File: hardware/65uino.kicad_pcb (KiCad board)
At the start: 2 copper layers, 74.9 x 53.3 mm, 55 parts, among them J1 Barrel_Jack_MountingPin, J2 USB_B_Micro, J3 OLED, SW1 RST, SW2 BTN, U1 R6507, U2 NC/74HC04, U3 6532, U4 w27C512, U5 MIC5504-3.3YM5, U6 LM1117-5.0, U7 SN74LVC1G14DBVR, X1 1MHz, Y1 NC/1Mhz

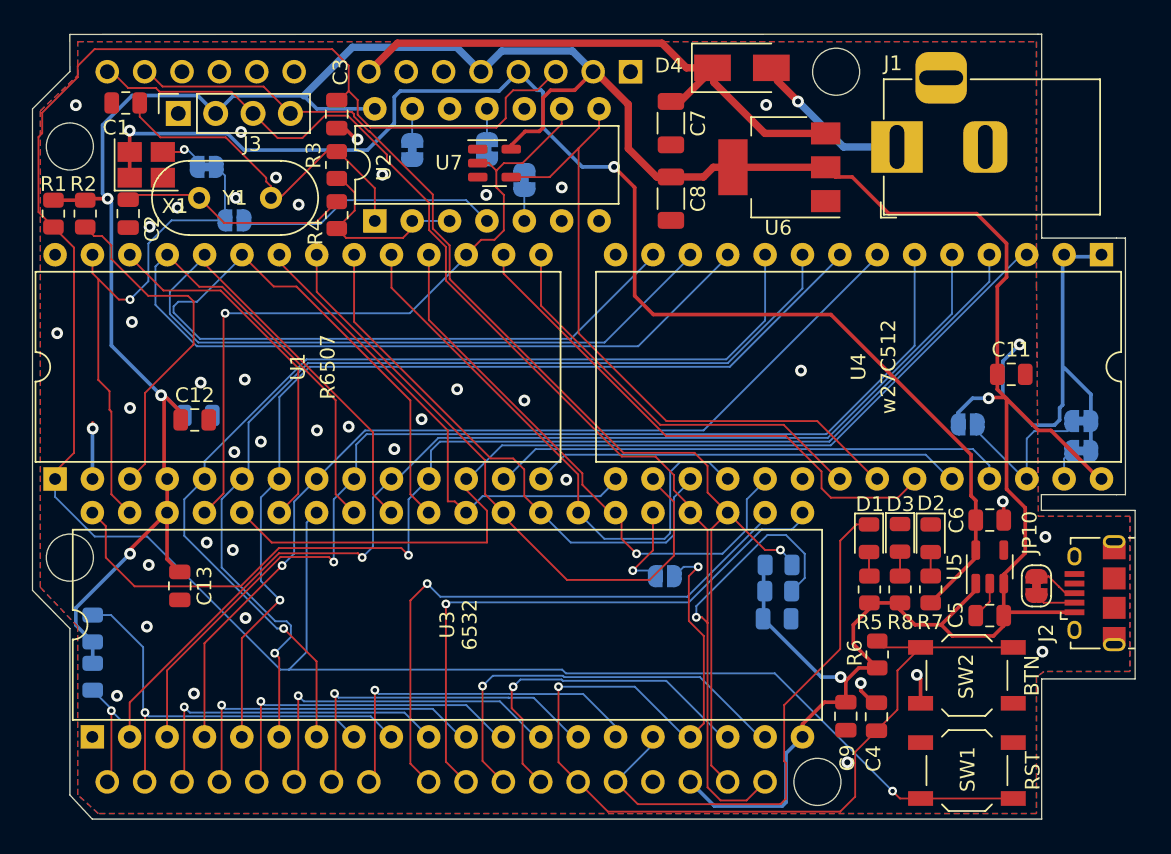
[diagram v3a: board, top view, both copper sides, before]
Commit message: Revision 1 - UART & Clock Divider
UART, Clock Divider, extra address decoding and bus headers added - a full-fledged 6502 computer with an Uno footprint!
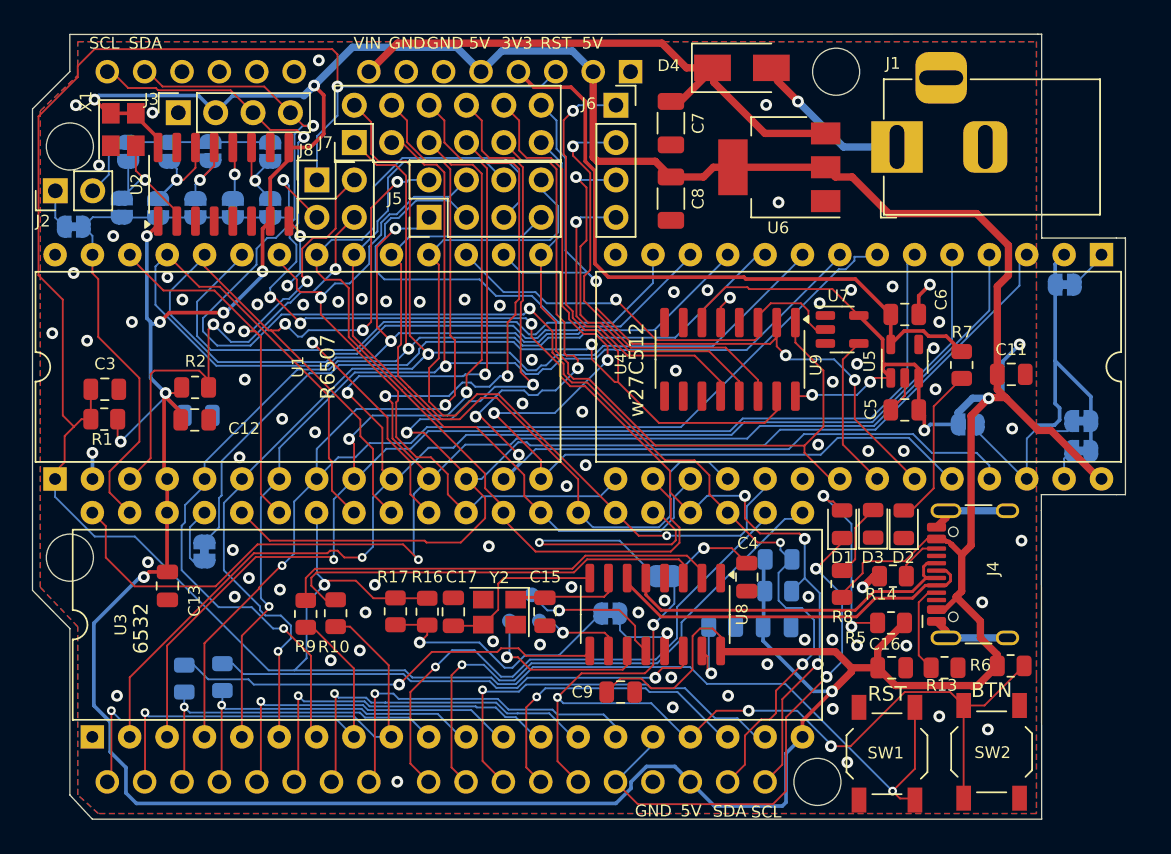
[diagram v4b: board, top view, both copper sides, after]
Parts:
- removed C1, C2: NC/30pF, Capacitor_SMD:C_0805_2012Metric
- removed Y1: NC/1Mhz, Crystal:Crystal_HC49-U_Vertical
- added C15: 22p, Capacitor_SMD:C_0805_2012Metric, F.Cu at (136.8, 87.8)
- added C16: 1uF, Capacitor_SMD:C_0805_2012Metric, F.Cu at (160.3, 91.6)
- added C17: 22p, Capacitor_SMD:C_0805_2012Metric, F.Cu at (130.6, 87.8)
- added J4: USB2.0_16P, Connector_USB:USB_C_Receptacle_HCTL_HC-TYPE-C-16P-01A, F.Cu at (167.1, 85.2)
- added J5: Databus, Connector_PinHeader_2.54mm:PinHeader_2x04_P2.54mm_Vertical, F.Cu at (128.9, 61.0)
- added J6: Chip select, Connector_PinSocket_2.54mm:PinSocket_1x04_P2.54mm_Vertical, F.Cu at (141.6, 53.3)
- added J7: Addressbus, Connector_PinHeader_2.54mm:PinHeader_2x06_P2.54mm_Vertical, F.Cu at (123.8, 55.9)
- added J8: Signals, Connector_PinHeader_2.54mm:PinHeader_2x02_P2.54mm_Vertical, F.Cu at (121.3, 58.4)
- added JP11: SolderJumper_2_Bridged, Jumper:SolderJumper-2_P1.3mm_Open_RoundedPad1.0x1.5mm, B.Cu at (108.5, 56.5)
- added JP12: SolderJumper_2_Bridged, Jumper:SolderJumper-2_P1.3mm_Open_RoundedPad1.0x1.5mm, B.Cu at (111.3, 56.5)
- added JP13: SolderJumper_2_Bridged, Jumper:SolderJumper-2_P1.3mm_Open_RoundedPad1.0x1.5mm, B.Cu at (114.0, 56.5)
- added JP14: SolderJumper_2_Bridged, Jumper:SolderJumper-2_P1.3mm_Open_RoundedPad1.0x1.5mm, B.Cu at (118.1, 56.5)
- added JP15: SolderJumper_2_Bridged, Jumper:SolderJumper-2_P1.3mm_Bridged_RoundedPad1.0x1.5mm, B.Cu at (104.8, 61.6)
- added JP16: SolderJumper_2_Bridged, Jumper:SolderJumper-2_P1.3mm_Bridged_RoundedPad1.0x1.5mm, B.Cu at (141.2, 87.9)
- added JP17: SolderJumper_2_Bridged, Jumper:SolderJumper-2_P1.3mm_Bridged_RoundedPad1.0x1.5mm, B.Cu at (113.6, 83.7)
- added R13: 5k1, Resistor_SMD:R_0805_2012Metric, F.Cu at (163.9, 91.6)
- added R14: 5k1, Resistor_SMD:R_0805_2012Metric, F.Cu at (160.4, 85.3)
- added R15: NC, Resistor_SMD:R_0805_2012Metric, B.Cu at (148.8, 88.8)
- added R16: 1k, Resistor_SMD:R_0805_2012Metric, F.Cu at (128.8, 87.8)
- added R17: 1k, Resistor_SMD:R_0805_2012Metric, F.Cu at (126.6, 87.7)
- added TP1: ~{RI}, TestPoint:TestPoint_Pad_D1.0mm, B.Cu at (134.4, 88.4)
- added TP2: ~{DCD}, TestPoint:TestPoint_Pad_D1.0mm, B.Cu at (135.9, 86.6)
- added TP3: ~{DSR}, TestPoint:TestPoint_Pad_D1.0mm, B.Cu at (136.4, 88.4)
- added U8: CH340G, Package_SO:SOIC-16_3.9x9.9mm_P1.27mm, F.Cu at (144.3, 87.9)
- added U9: 74HC138, Package_SO:SOP-16_3.9x9.9mm_P1.27mm, F.Cu at (149.4, 70.6)
- added Y2: 12MHz, Crystal:Crystal_SMD_3225-4Pin_3.2x2.5mm, F.Cu at (133.7, 87.8)
- D3: value WHITE LED -> RED LED
- J1: value Barrel_Jack_MountingPin -> Barrel
- J2: value USB_B_Micro -> GPCO; footprint Connector_USB:USB_Micro-B_Amphenol_10118194_Horizontal -> Connector_PinHeader_2.54mm:PinHeader_1x02_P2.54mm_Vertical
- JP10: moved to B.Cu
- JP3, JP4, JP5: footprint Jumper:SolderJumper-2_P1.3mm_Bridged_RoundedPad1.0x1.5mm -> Jumper:SolderJumper-2_P1.3mm_Open_RoundedPad1.0x1.5mm
- R10, R9: value NC -> 1k; moved to F.Cu
- R3: value NC/1M -> NC; moved to B.Cu
- R4: value NC/470 -> NC; moved to B.Cu
- U2: value NC/74HC04 -> 74HC161; footprint Package_DIP:DIP-14_W7.62mm -> Package_SO:SOP-16_3.9x9.9mm_P1.27mm
- U6: value LM1117-5.0 -> AMS1117-5.0
- X1: value 1MHz -> 8MHz; footprint Oscillator:Oscillator_SMD_SeikoEpson_SG210-4Pin_2.5x2.0mm_HandSoldering -> Crystal:Crystal_SMD_3225-4Pin_3.2x2.5mm
- moved J2 75.8 mm to (103.5, 59.2)
- moved R3 36.4 mm to (112.3, 92.3)
- moved R4 32.3 mm to (114.9, 92.2)
- moved U7 26.2 mm to (157.0, 68.6)
- moved C3 24.5 mm to (106.9, 72.6), turned to 180 degrees
- moved JP5 22.7 mm to (110.5, 60.3), turned to -90 degrees
- moved JP10 20.6 mm to (172.1, 65.5), turned to 0 degrees
- moved JP3 17.4 mm to (118.1, 60.3)
- moved R10 16.5 mm to (122.6, 87.9), turned to 90 degrees
- moved R7 15.4 mm to (165.1, 71.0), turned to 90 degrees
- moved C9 15.4 mm to (141.9, 93.2), turned to 0 degrees
- moved JP4 15.2 mm to (113.0, 60.3), turned to -90 degrees
- moved C6 15.1 mm to (161.2, 67.6)
- moved C5 15.1 mm to (161.2, 74.0)
- moved U5 15.1 mm to (161.2, 70.7)
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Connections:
- net Net-(R2-Pad2) renamed /RDY
- net Net-(U1-Pad26) renamed /~{RW}
- J2 pad 1: +5V -> Net-(J2-Pin_1)
- J2 pad 2: Net-(J2-Pad2) -> Net-(J2-Pin_2)
- JP10 pad 1: Net-(J2-Pad2) -> GND
- JP10 pad 2: Net-(J2-Pad3) -> Net-(JP10-B)
- JP3 pad 1: GND -> 500KHz
- JP3 pad 2: Net-(JP3-Pad2) -> /PHI0
- JP4 pad 1: GND -> 2Mhz
- JP4 pad 2: Net-(JP4-Pad2) -> /PHI0
- JP5 pad 1: GND -> 4Mhz
- JP5 pad 2: Net-(JP5-Pad2) -> /PHI0
- JP6 pad 1: Net-(JP6-Pad1) -> 8Mhz
- JP7 pad 1: Net-(JP7-Pad1) -> 1Mhz
- R10 pad 2: +5V -> /RXD
- R3 pad 1: Net-(R3-Pad1) -> /PA2/D2
- R3 pad 2: Net-(C1-Pad1) -> /~{CTS}
- R4 pad 1: Net-(R3-Pad1) -> /PA3/D3
- R4 pad 2: Net-(C2-Pad1) -> /~{RTS}
- R9 pad 2: +5V -> /TXD
- U2 pad 1: Net-(C1-Pad1) -> +5V
- U2 pad 11: Net-(JP5-Pad2) -> 500KHz
- U2 pad 12: unconnected-(U2-Pad12) -> 1Mhz
- U2 pad 13: Net-(JP4-Pad2) -> 2Mhz
- U2 pad 14: +5V -> 4Mhz
- U2 pad 2: Net-(R3-Pad1) -> 8Mhz
- U2 pad 3: Net-(R3-Pad1) -> unconnected-(U2-D0-Pad3)
- U2 pad 4: Net-(JP6-Pad1) -> unconnected-(U2-D1-Pad4)
- U2 pad 5: Net-(JP3-Pad2) -> unconnected-(U2-D2-Pad5)
- U2 pad 7: GND -> +5V
- U2 pad 8: Net-(U2-Pad8) -> GND
- U2 pad 9: A12 -> +5V
- U3 pad 37: A12 -> Net-(JP17-A)
- U4 pad 1: GND -> Net-(JP10-B)
- U4 pad 22: Net-(U2-Pad8) -> Net-(U4-~{OE})
- U7 pad 4: Net-(U2-Pad8) -> Net-(U4-~{OE})
- X1 pad 1: +3V3 -> +5V
- X1 pad 3: Net-(JP7-Pad1) -> 8Mhz
- X1 pad 4: +3V3 -> +5V
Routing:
- net +5V: track 237.0 -> 355.5 mm, vias 5 -> 14
- net /6532_CS: track 0.00 -> 75.5 mm, vias 0 -> 2
- net Net-(U2-Pad8): track 45.7 -> 0.00 mm
- net +3V3: track 91.2 -> 46.0 mm, vias 2 -> 0
- net A5: track 74.8 -> 114.9 mm, vias 1 -> 3
- net A9: track 29.4 -> 67.0 mm, vias 0 -> 2
- net A7: track 66.1 -> 103.4 mm, vias 0 -> 2
- net A6: track 78.2 -> 113.9 mm, vias 1 -> 3
- net A3: track 64.8 -> 100.1 mm, vias 1 -> 2
- net A8: track 35.2 -> 69.5 mm, vias 0 -> 3
- net /~{RTS}: track 0.00 -> 33.7 mm, vias 0 -> 1
- net A4: track 74.5 -> 107.1 mm, vias 1 -> 3
- net /TXD: track 0.00 -> 29.5 mm
- net /RXD: track 0.00 -> 29.5 mm
- net /~{CTS}: track 0.00 -> 29.4 mm, vias 0 -> 1
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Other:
- board size 74.9 x 53.3 mm -> 74.3 x 53.3 mm
- board text added: "$0000"
- board text added: "$0400"
- board text added: "$0800"
- board text added: "$0C00"
- board text added: ".5M"
- board text added: "18V Max!"
- board text added: "1M"
- board text added: "2M"
- board text added: "4M"
- board text added: "6532 IRQ"
- board text added: "6532 ~{CS}"
- board text added: "65uino rev 1 ABNielsen.com/65uino"
- board text added: "8MHz"
- board text added: "A0"
- board text added: "A1"
- board text added: "A10"
- board text added: "A11"
- board text added: "D0"
- board text added: "D1"
- board text added: "D6"
- board text added: "D7"
- board text added: "PB6"
- board text added: "RDY"
- board text added: "~{DTR}"
- board text removed: "65uino rev 0 ABNielsen.com/65uino"

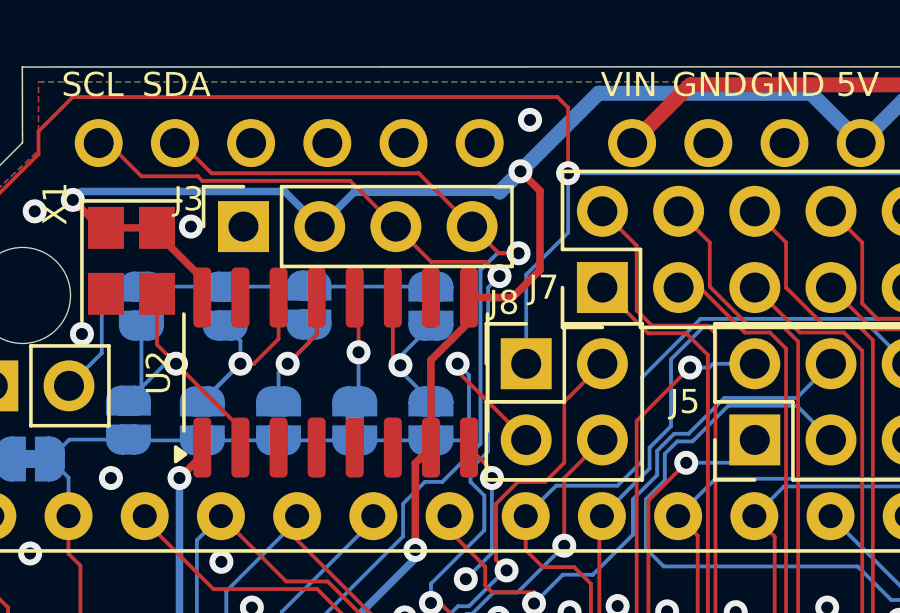
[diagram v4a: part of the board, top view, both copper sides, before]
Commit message: Rev1 Gerber Fix
Connect U2 pin 9 and 10 for stable oscillator performance without solder blob
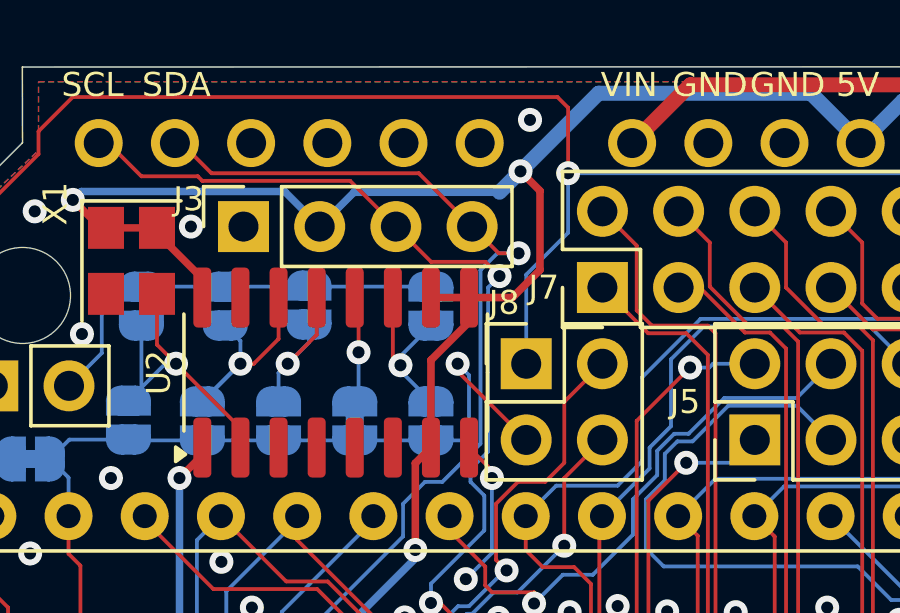
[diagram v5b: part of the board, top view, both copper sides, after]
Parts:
- R7: value 15k -> 22k
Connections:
- U2 pad 10: unconnected-(U2-CET-Pad10) -> +5V
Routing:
- net +5V: track 355.5 -> 356.7 mm

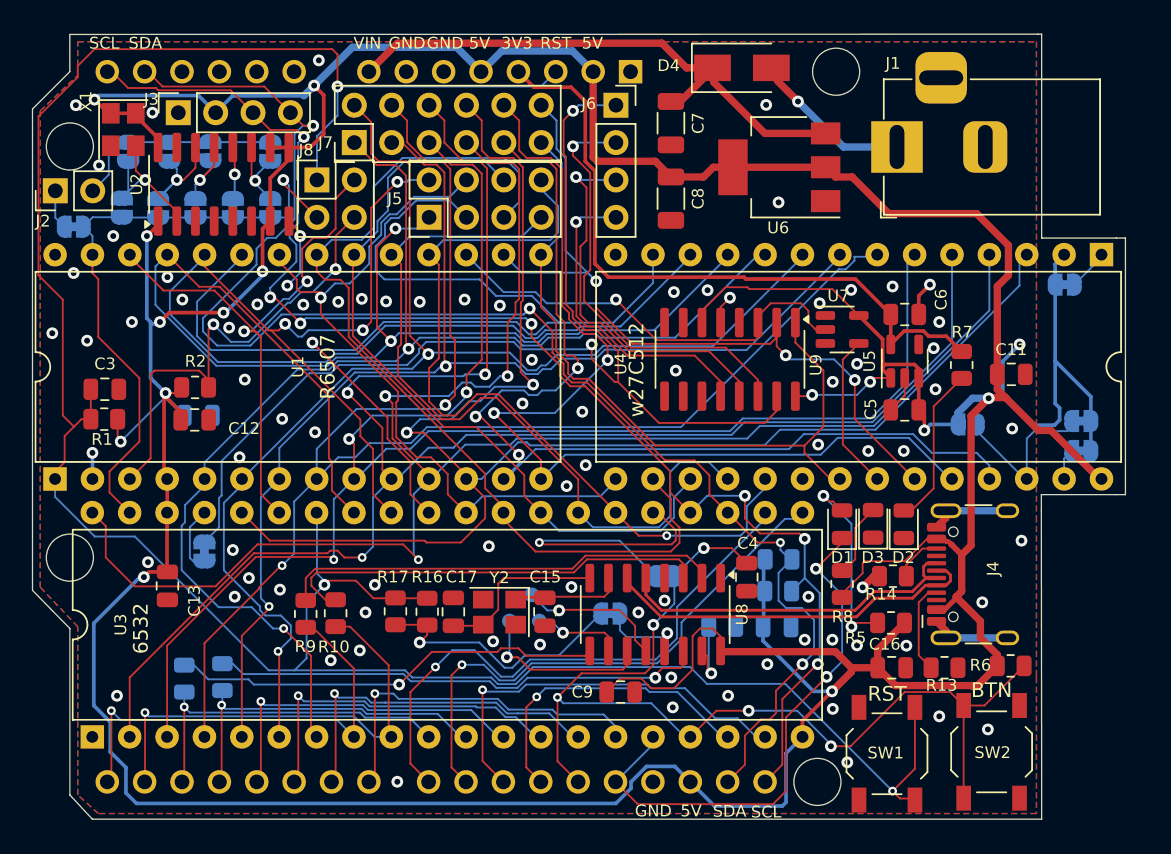
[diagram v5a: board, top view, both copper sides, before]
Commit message: Rev 1.1
Rev 1.1 - working i2c scanner, default baud rate 4800, SOT23 EEPROM added
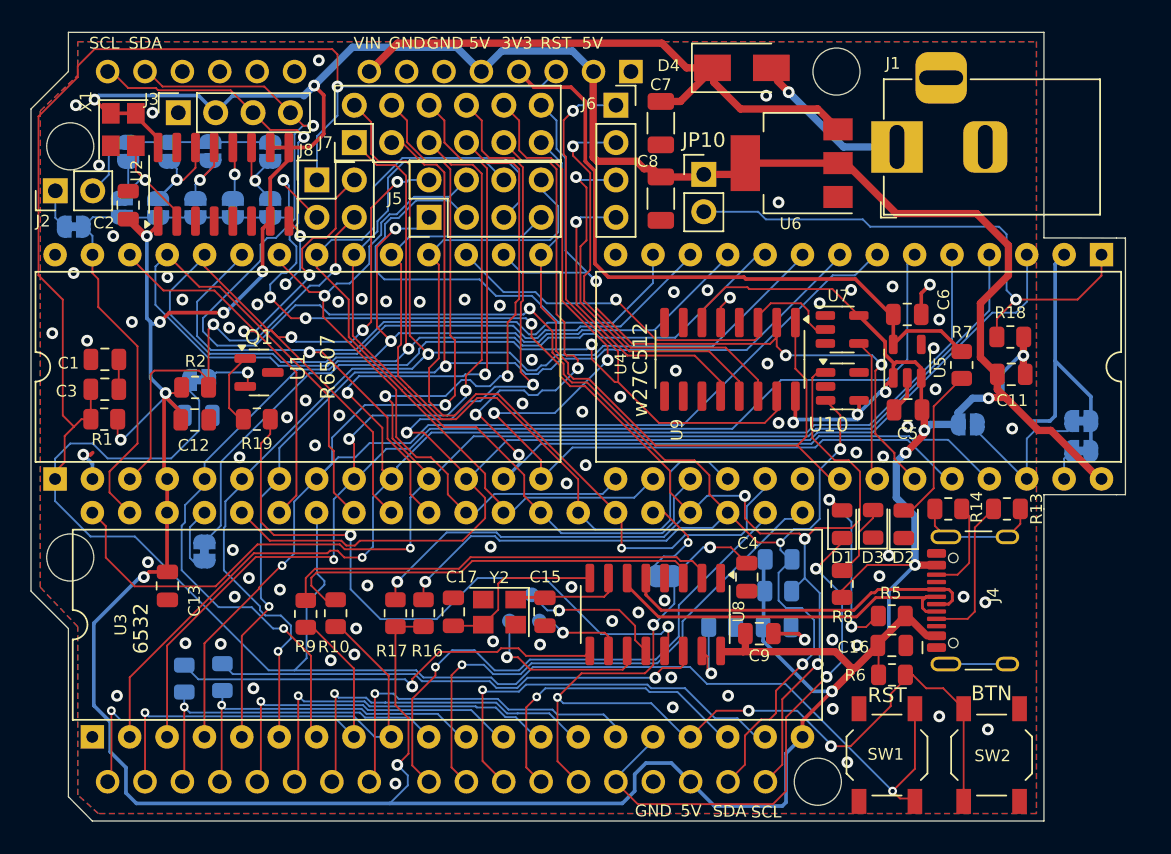
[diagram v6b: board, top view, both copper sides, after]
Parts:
- added C1: 100nF, Capacitor_SMD:C_0805_2012Metric, F.Cu at (106.9, 70.6)
- added C2: 100nF, Capacitor_SMD:C_0805_2012Metric, F.Cu at (108.5, 60.1)
- added Q1: MMBT3906, Package_TO_SOT_SMD:SOT-23, F.Cu at (117.3, 71.5)
- added R18: 22k, Resistor_SMD:R_0805_2012Metric, F.Cu at (168.4, 69.1)
- added R19: 1k, Resistor_SMD:R_0805_2012Metric, F.Cu at (117.2, 74.7)
- added U10: 24C64S, Package_TO_SOT_SMD:SOT-23-5, F.Cu at (157.0, 72.5)
- JP10: value SolderJumper_2_Bridged -> Jumper; footprint Jumper:SolderJumper-2_P1.3mm_Bridged_RoundedPad1.0x1.5mm -> Connector_PinHeader_2.54mm:PinHeader_1x02_P2.54mm_Vertical; moved to F.Cu
- R16, R17: value 1k -> 5k1
- moved JP16 32.1 mm to (113.3, 72.0)
- moved JP10 25.6 mm to (147.6, 58.0)
- moved R13 11.6 mm to (168.2, 80.8)
- moved C9 10.2 mm to (151.3, 89.2)
- moved R6 8.09 mm to (160.4, 92.0)
- moved R14 5.92 mm to (164.2, 80.8)
- moved J4 1.78 mm to (167.1, 87.0)
- moved C16 1.52 mm to (160.3, 90.0)
- moved U6 0.88 mm to (153.5, 57.3)
- moved C7 0.69 mm to (144.7, 54.6)
- moved C8 0.69 mm to (144.7, 59.7)
- moved R5 0.47 mm to (160.3, 88.0)
- moved R16 0.27 mm to (128.5, 87.9)
- moved C5 0.22 mm to (161.4, 74.0)
- moved SW2 0.22 mm to (167.1, 97.5)
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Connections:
- C3 pad 1: GND -> Net-(C1-Pad2)
- JP10 pad 1: GND -> +5V
- JP16 pad 1: /~{DTR} -> Net-(JP16-A)
- JP16 pad 2: Net-(JP16-B) -> /RST
- R16 pad 1: /RST -> /SDA
- R16 pad 2: Net-(JP16-B) -> +5V
- R17 pad 1: /RST -> /SCL
- R17 pad 2: Net-(JP16-B) -> +5V
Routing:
- net /SCL: track 93.9 -> 133.4 mm, vias 7 -> 8
- net /~{DTR}: track 5.95 -> 44.5 mm, vias 1 -> 2
- net /SDA: track 101.4 -> 138.3 mm, vias 4 -> 6
- net Net-(JP10-B): track 2.62 -> 36.9 mm, vias 0 -> 1
- net Net-(JP16-B): track 18.1 -> 0.00 mm, vias 1 -> 0
- net Net-(JP9-B): track 20.2 -> 6.53 mm
- net /RST: track 171.3 -> 180.3 mm, vias 3 -> 2
- net D4: track 63.0 -> 54.9 mm
- net Net-(Q1-B): track 0.00 -> 4.89 mm
- net Net-(J4-CC1): track 5.72 -> 10.3 mm
- net GND: track 53.6 -> 57.8 mm, vias 85 -> 88
- net /PB6/D12: track 70.1 -> 66.3 mm
- net Net-(JP16-A): track 0.00 -> 3.64 mm, vias 0 -> 1
- net Net-(J4-CC2): track 3.28 -> 6.44 mm
- net /VIN: track 38.2 -> 40.3 mm
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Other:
- board size 74.3 x 53.3 mm -> 74.4 x 53.6 mm
- board text added: "65uino rev 1.1 ABNielsen.com/65uino"
- board text added: "JP10 ROM Bank"
- board text removed: "65uino rev 1 ABNielsen.com/65uino"
- board text removed: "~{DTR}"
